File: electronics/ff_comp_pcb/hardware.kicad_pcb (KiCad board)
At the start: 4 copper layers, 62 x 37 mm, 98 parts, among them J1 Micro_SD_Card_Det_Hirose_DM3AT, J2 USB_A, J3 Conn_01x07_Female, Q1 Q_PMOS_GDS, Q2 Q_NPN_BEC, U1 AS4C512M16D3L-12BIN, U2 A33, U3 FSUSB42MUX, U4 RTL8188CUS, U5 RTL8188CUS, Y1 24Mhz, Y2 32.768khz

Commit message: Added gerbers for R0.1 comp pcb.
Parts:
- removed H1: MountingHole, MountingHole:MountingHole_3.2mm_M3
- added J4: Conn_01x03_Male, Connector_PinHeader_2.54mm:PinHeader_1x03_P2.54mm_Vertical, F.Cu at (89.2, 122.5)
- Q1: value Q_PMOS_GDS -> Q_PMOS_GSD
- moved Q1 0.15 mm to (92.8, 102.0), turned to 180 degrees
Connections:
- Q1 pad 2: Net-(J2-Pad1) -> +5V
- Q1 pad 3: +5V -> Net-(J2-Pad1)
- U1 pad J1: Net-(U1-PadJ1) -> (no net)
- U1 pad J9: Net-(U1-PadJ9) -> (no net)
- U1 pad L1: Net-(U1-PadL1) -> (no net)
- U1 pad L9: Net-(U1-PadL9) -> (no net)
- U2 pad A10: Net-(U2-PadA10) -> (no net)
- U2 pad A11: Net-(U2-PadA11) -> (no net)
- U2 pad A12: Net-(U2-PadA12) -> (no net)
- U2 pad A13: Net-(U2-PadA13) -> (no net)
- U2 pad A14: Net-(U2-PadA14) -> (no net)
- U2 pad A15: Net-(U2-PadA15) -> (no net)
- U2 pad A16: Net-(U2-PadA16) -> (no net)
- U2 pad A2: Net-(U2-PadA2) -> (no net)
- U2 pad A3: Net-(U2-PadA3) -> (no net)
- U2 pad A4: Net-(U2-PadA4) -> (no net)
- U2 pad A5: Net-(U2-PadA5) -> (no net)
- U2 pad A6: Net-(U2-PadA6) -> (no net)
- U2 pad A7: Net-(U2-PadA7) -> (no net)
- U2 pad A8: Net-(U2-PadA8) -> (no net)
- U2 pad A9: Net-(U2-PadA9) -> (no net)
- U2 pad B10: Net-(U2-PadB10) -> (no net)
- U2 pad B11: Net-(U2-PadB11) -> (no net)
- U2 pad B13: Net-(U2-PadB13) -> (no net)
- U2 pad B14: Net-(U2-PadB14) -> (no net)
- U2 pad B15: Net-(U2-PadB15) -> (no net)
- U2 pad B16: Net-(U2-PadB16) -> (no net)
- U2 pad B2: Net-(U2-PadB2) -> (no net)
- U2 pad B3: Net-(U2-PadB3) -> (no net)
- U2 pad B4: Net-(U2-PadB4) -> (no net)
- U2 pad B5: Net-(U2-PadB5) -> (no net)
- U2 pad B6: Net-(U2-PadB6) -> (no net)
- U2 pad B7: Net-(U2-PadB7) -> (no net)
- U2 pad B8: Net-(U2-PadB8) -> (no net)
- U2 pad B9: Net-(U2-PadB9) -> (no net)
- U2 pad C10: Net-(U2-PadC10) -> (no net)
- U2 pad C11: Net-(U2-PadC11) -> (no net)
- U2 pad C12: Net-(U2-PadC12) -> (no net)
- U2 pad C13: Net-(U2-PadC13) -> (no net)
- U2 pad C14: Net-(U2-PadC14) -> (no net)
- U2 pad C15: Net-(U2-PadC15) -> (no net)
- U2 pad C16: Net-(U2-PadC16) -> (no net)
- U2 pad C17: Net-(U2-PadC17) -> (no net)
- U2 pad C3: Net-(U2-PadC3) -> (no net)
- U2 pad C4: Net-(U2-PadC4) -> (no net)
- U2 pad C5: Net-(U2-PadC5) -> (no net)
- U2 pad C6: Net-(U2-PadC6) -> (no net)
- U2 pad D10: Net-(U2-PadD10) -> (no net)
- U2 pad D11: Net-(U2-PadD11) -> (no net)
- U2 pad D12: Net-(U2-PadD12) -> (no net)
- U2 pad D13: Net-(U2-PadD13) -> (no net)
- U2 pad D14: Net-(U2-PadD14) -> (no net)
- U2 pad D15: Net-(U2-PadD15) -> (no net)
- U2 pad D16: Net-(U2-PadD16) -> (no net)
- U2 pad D17: Net-(U2-PadD17) -> (no net)
- U2 pad D3: Net-(U2-PadD3) -> (no net)
- U2 pad D4: Net-(U2-PadD4) -> (no net)
- U2 pad D5: Net-(U2-PadD5) -> (no net)
- U2 pad D6: Net-(U2-PadD6) -> (no net)
- U2 pad E14: Net-(U2-PadE14) -> (no net)
- U2 pad E15: Net-(U2-PadE15) -> (no net)
- U2 pad E16: Net-(U2-PadE16) -> (no net)
- U2 pad E17: Net-(U2-PadE17) -> (no net)
- U2 pad F14: Net-(U2-PadF14) -> (no net)
- U2 pad F15: Net-(U2-PadF15) -> (no net)
- U2 pad F16: Net-(U2-PadF16) -> (no net)
- U2 pad F17: Net-(U2-PadF17) -> (no net)
- U2 pad G15: Net-(U2-PadG15) -> (no net)
- U2 pad H14: Net-(U2-PadH14) -> (no net)
- U2 pad H15: Net-(U2-PadH15) -> (no net)
- U2 pad H16: Net-(U2-PadH16) -> (no net)
- U2 pad J14: Net-(U2-PadJ14) -> (no net)
- U2 pad J15: Net-(U2-PadJ15) -> (no net)
- U2 pad J16: Net-(U2-PadJ16) -> (no net)
- U2 pad J17: Net-(U2-PadJ17) -> (no net)
- U2 pad K14: Net-(U2-PadK14) -> (no net)
- U2 pad K15: Net-(U2-PadK15) -> (no net)
- U2 pad L14: Net-(U2-PadL14) -> (no net)
- U2 pad L15: Net-(U2-PadL15) -> (no net)
- U2 pad L7: Net-(U2-PadL7) -> (no net)
- U2 pad M15: Net-(U2-PadM15) -> (no net)
- U2 pad M16: Net-(U2-PadM16) -> (no net)
- U2 pad M17: Net-(U2-PadM17) -> (no net)
- U2 pad N15: Net-(U2-PadN15) -> (no net)
- U2 pad N16: Net-(U2-PadN16) -> (no net)
- U2 pad N17: Net-(U2-PadN17) -> (no net)
- U2 pad N5: Net-(U2-PadN5) -> (no net)
- U2 pad N7: Net-(U2-PadN7) -> (no net)
- U2 pad P10: Net-(U2-PadP10) -> (no net)
- U2 pad P11: Net-(U2-PadP11) -> (no net)
- U2 pad P12: Net-(U2-PadP12) -> (no net)
- U2 pad P13: Net-(U2-PadP13) -> (no net)
- U2 pad P14: Net-(U2-PadP14) -> (no net)
- U2 pad P15: Net-(U2-PadP15) -> (no net)
- U2 pad P16: Net-(U2-PadP16) -> (no net)
- U2 pad P4: Net-(U2-PadP4) -> (no net)
- U2 pad P5: Net-(U2-PadP5) -> (no net)
- U2 pad P6: Net-(U2-PadP6) -> (no net)
- U2 pad P7: Net-(U2-PadP7) -> (no net)
- U2 pad P8: Net-(U2-PadP8) -> (no net)
- U2 pad P9: Net-(U2-PadP9) -> (no net)
- U2 pad R10: Net-(U2-PadR10) -> (no net)
- U2 pad R11: Net-(U2-PadR11) -> (no net)
- U2 pad R12: Net-(U2-PadR12) -> (no net)
- U2 pad R13: Net-(U2-PadR13) -> (no net)
- U2 pad R14: Net-(U2-PadR14) -> (no net)
- U2 pad R15: Net-(U2-PadR15) -> (no net)
- U2 pad R4: Net-(U2-PadR4) -> (no net)
- U2 pad R5: Net-(U2-PadR5) -> (no net)
- U2 pad R6: Net-(U2-PadR6) -> (no net)
- U2 pad R7: Net-(U2-PadR7) -> (no net)
- U2 pad R8: Net-(U2-PadR8) -> (no net)
- U2 pad R9: Net-(U2-PadR9) -> (no net)
- U2 pad T10: Net-(U2-PadT10) -> (no net)
- U2 pad T11: Net-(U2-PadT11) -> (no net)
- U2 pad T12: Net-(U2-PadT12) -> (no net)
- U2 pad T13: Net-(U2-PadT13) -> (no net)
- U2 pad T14: Net-(U2-PadT14) -> (no net)
- U2 pad T15: Net-(U2-PadT15) -> (no net)
- U2 pad T5: Net-(U2-PadT5) -> (no net)
- U2 pad T6: Net-(U2-PadT6) -> (no net)
- U2 pad T7: Net-(U2-PadT7) -> (no net)
- U2 pad T8: Net-(U2-PadT8) -> (no net)
- U2 pad T9: Net-(U2-PadT9) -> (no net)
- U2 pad U10: Net-(U2-PadU10) -> (no net)
- U2 pad U11: Net-(U2-PadU11) -> (no net)
- U2 pad U12: Net-(U2-PadU12) -> (no net)
- U2 pad U14: Net-(U2-PadU14) -> (no net)
- U2 pad U15: Net-(U2-PadU15) -> (no net)
- U2 pad U5: Net-(U2-PadU5) -> (no net)
- U2 pad U6: Net-(U2-PadU6) -> (no net)
- U2 pad U7: Net-(U2-PadU7) -> (no net)
- U2 pad U8: Net-(U2-PadU8) -> (no net)
- U2 pad U9: Net-(U2-PadU9) -> (no net)
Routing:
- net /gpio/UART0_RX: track 0.00 -> 35.1 mm
- net /gpio/UART0_TX: track 0.00 -> 32.0 mm
- net Net-(Q1-Pad1): track 8.69 -> 11.6 mm
- net Net-(J2-Pad1): track 10.6 -> 12.3 mm
- net +1V1: track 16.7 -> 15.4 mm
- net GND: track 6.46 -> 7.17 mm, vias 47 -> 46

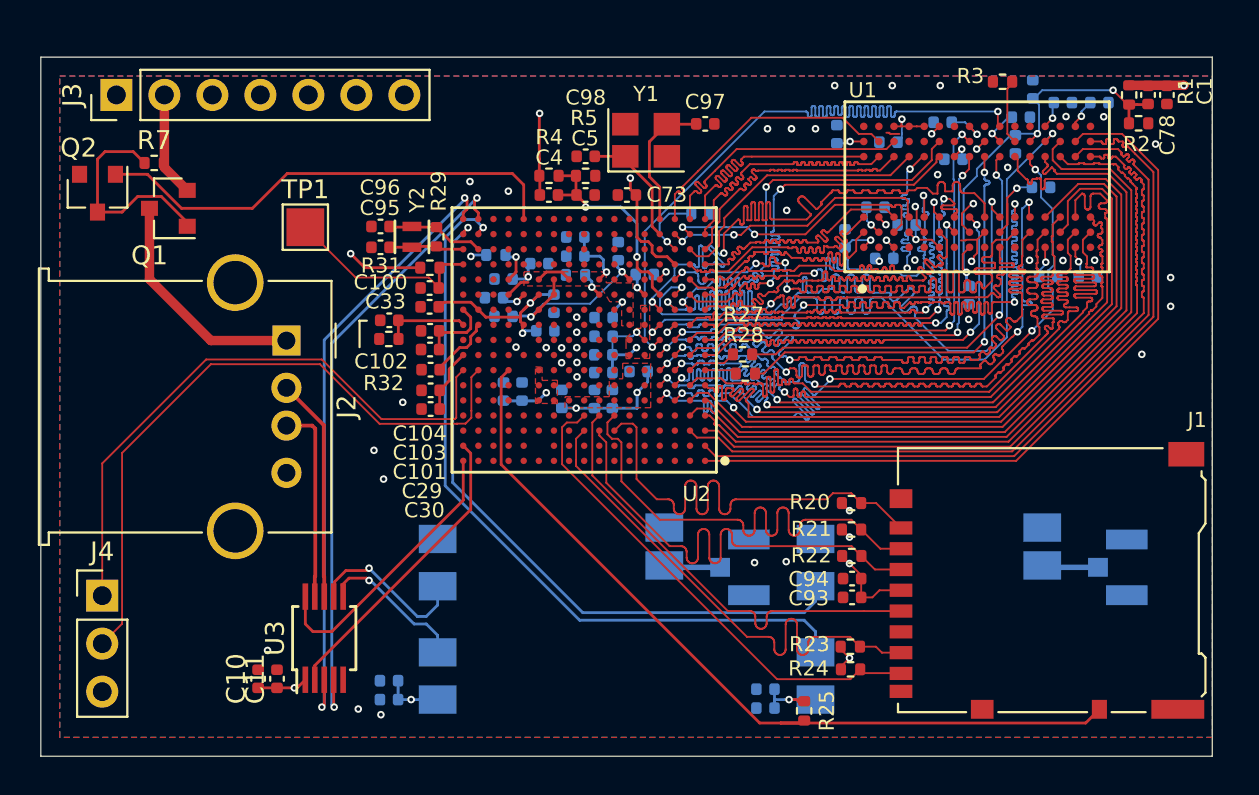
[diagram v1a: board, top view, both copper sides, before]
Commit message: Headers were not aligned in comp_pcb, alligned them, created R0.2 and imported into assembly.
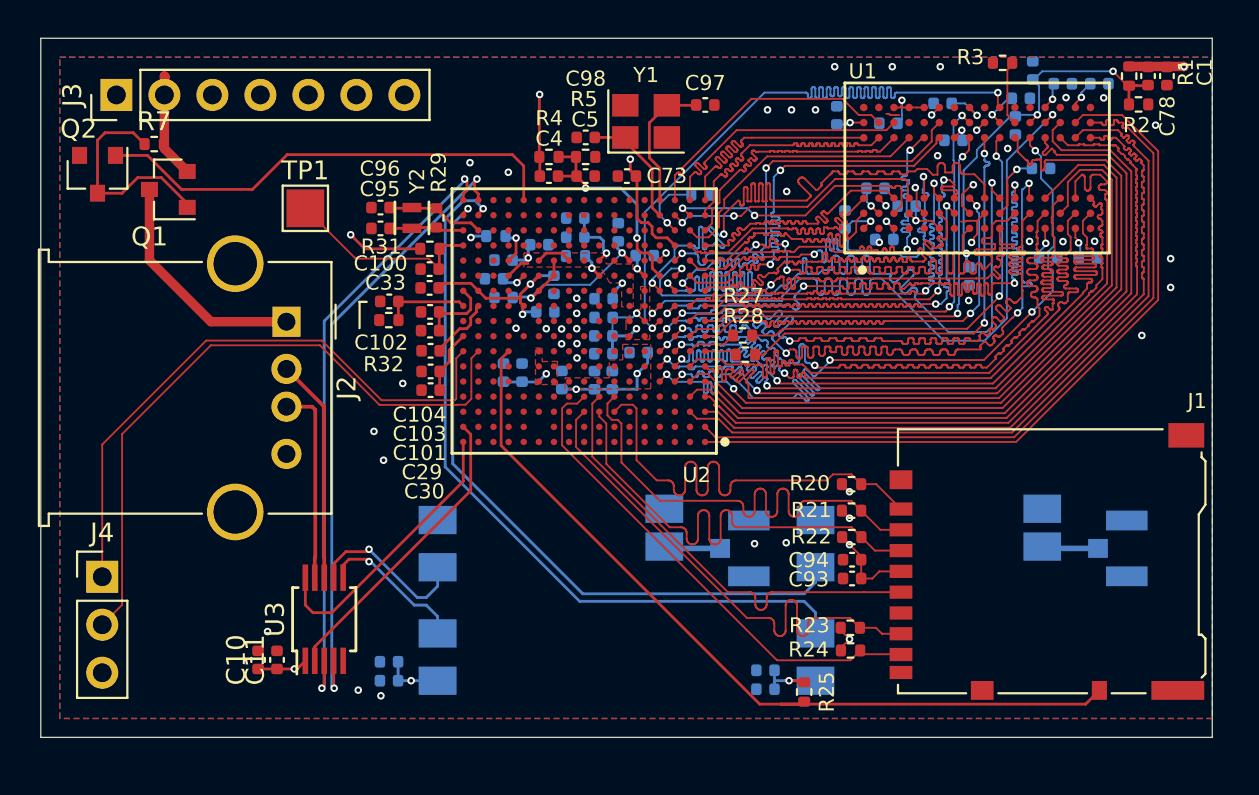
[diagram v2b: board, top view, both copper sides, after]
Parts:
- moved AE1 1.00 mm to (123.0, 120.0)
- moved AE2 1.00 mm to (143.0, 120.0)
- moved C1 1.00 mm to (144.6, 95.0)
- moved C10 1.00 mm to (97.5, 125.9)
- moved C100 1.00 mm to (106.6, 105.2)
- moved C101 1.00 mm to (106.6, 109.5)
- moved C102 1.00 mm to (104.4, 106.9)
- moved C103 1.00 mm to (106.6, 108.5)
- moved C104 1.00 mm to (106.6, 107.5)
- moved C11 1.00 mm to (98.5, 125.9)
- moved C2 1.00 mm to (137.6, 97.6)
- moved C29 1.00 mm to (106.6, 110.6)
- moved C3 1.00 mm to (138.5, 94.7)
- moved C30 1.00 mm to (106.6, 111.6)
- moved C31 1.00 mm to (113.2, 106.0)
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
